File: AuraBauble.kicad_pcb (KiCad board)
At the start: 2 copper layers, 15 x 19 mm, 39 parts, among them J1 Bauble-Expando!, J2 USB_A, J3 SWD, SW1 KXT 321 LHS, U1 ATSAMD11D14A-M, U2 LP5912-3.3DRV, U3 74LVC1G02SE-7, U4 NXB0104GU12X, Y1 FC-135R

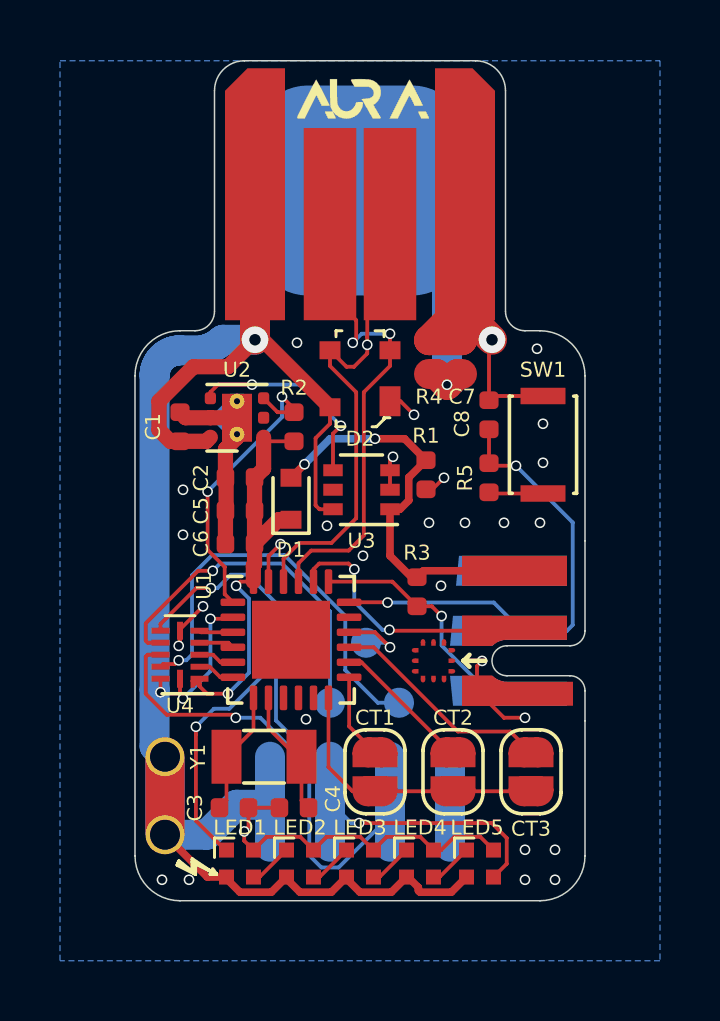
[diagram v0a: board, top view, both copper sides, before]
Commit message: Move BP1 a bit so it doesn't collide with expando silk.
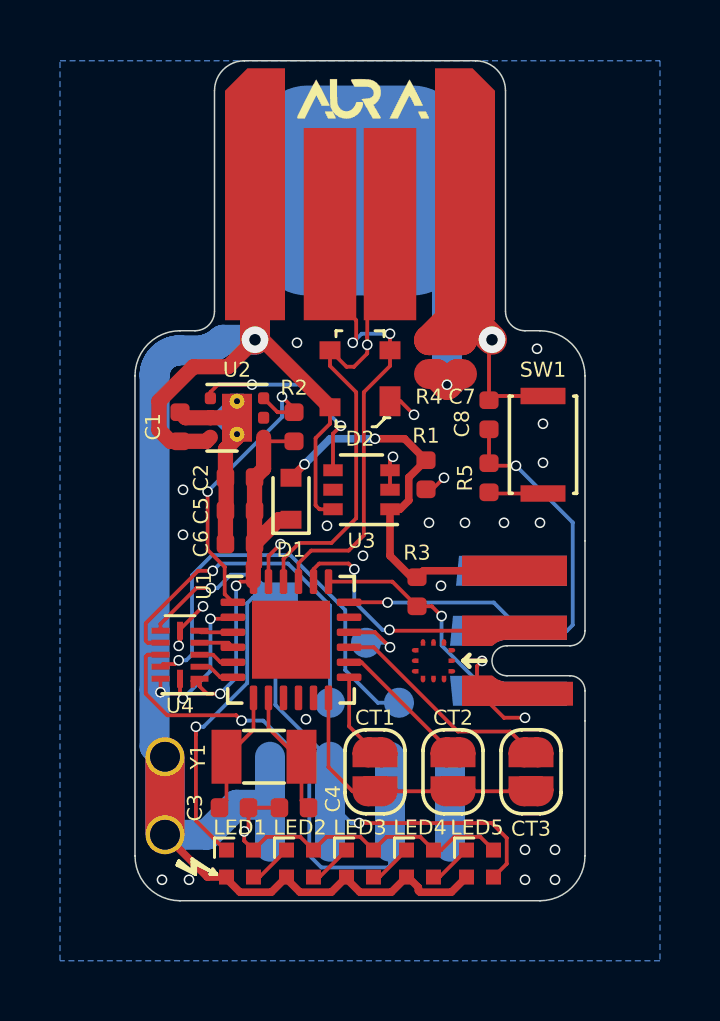
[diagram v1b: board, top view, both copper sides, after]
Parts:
- moved BP1 0.86 mm to (147.2, 68.6)
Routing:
- net /SCK_5V: track 15.2 -> 16.2 mm
- net VCC: track 14.2 -> 13.7 mm

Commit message: Cleanup some C & R values.
Adjusted C7 up slightly based on parts available. R1 moved from 100 MOhms to 1 MOhm to line up part with R4.
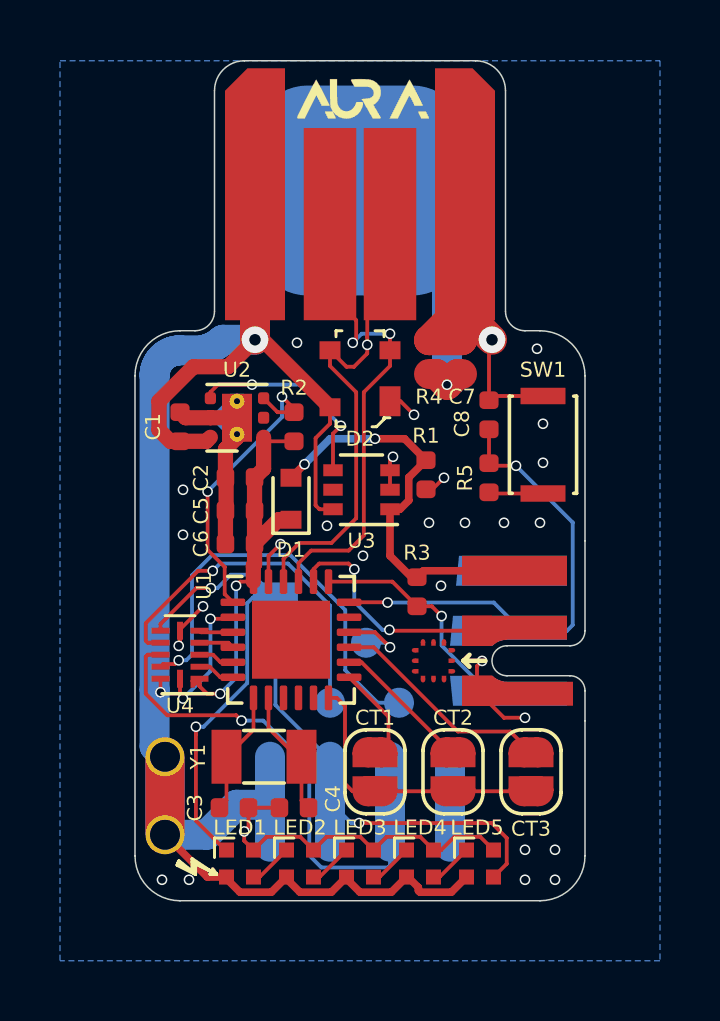
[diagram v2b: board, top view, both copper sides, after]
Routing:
- net GND: vias 30 -> 29
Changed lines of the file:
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@@
     (thickness 1.6)
     (drawings 30)
-    (tracks 440)
+    (tracks 442)
     (zones 0)
     (modules 39)
@@
   (title_block
     (title "Aura Bauble")
-    (date 2020-09-14)
+    (date 2020-09-15)
     (rev 0)
     (company cmd.wtf)
@@
     (38 B.Mask user hide)
     (39 F.Mask user hide)
-    (40 Dwgs.User user hide)
+    (40 Dwgs.User user)
     (41 Cmts.User user hide)
     (42 Eco1.User user hide)
@@
   (via (at 143.4 77.3) (size 0.3556) (drill 0.254) (layers F.Cu B.Cu) (net 3))
   (via (at 147.9 59.4) (size 0.3556) (drill 0.254) (layers F.Cu B.Cu) (net 3))
-  (via (at 148.2 71.95) (size 0.3556) (drill 0.254) (layers F.Cu B.Cu) (net 3))
   (via (at 152.7 67.5) (size 0.3556) (drill 0.254) (layers F.Cu B.Cu) (net 3))
   (via (at 150.1 66.5) (size 0.3556) (drill 0.254) (layers F.Cu B.Cu) (net 3))
@@
   (segment (start 153.1 74.35) (end 155.7 74.35) (width 0.127) (layer F.Cu) (net 10))
   (segment (start 149.752408 74.35) (end 150.5 74.35) (width 0.127) (layer F.Cu) (net 10))
-  (segment (start 148.95 73.547592) (end 149.752408 74.35) (width 0.127) (layer F.Cu) (net 10))
-  (segment (start 148.95 71.2375) (end 148.95 73.547592) (width 0.127) (layer F.Cu) (net 10))
-  (segment (start 149.6375 72.1875) (end 150.5 73.05) (width 0.127) (layer F.Cu) (net 11))
-  (segment (start 149.6375 70.55) (end 149.6375 72.1875) (width 0.127) (layer F.Cu) (net 11))
+  (segment (start 149.5 71.51) (end 149.5 74.097592) (width 0.127) (layer F.Cu) (net 10))
+  (segment (start 149.5 74.097592) (end 149.752408 74.35) (width 0.127) (layer F.Cu) (net 10))
+  (segment (start 148.95 71.2375) (end 149.2275 71.2375) (width 0.127) (layer F.Cu) (net 10))
+  (segment (start 149.2275 71.2375) (end 149.5 71.51) (width 0.127) (layer F.Cu) (net 10))
+  (segment (start 149.6375 70.55) (end 150.95 71.8625) (width 0.127) (layer F.Cu) (net 11))
+  (segment (start 150.95 72.6) (end 150.5 73.05) (width 0.127) (layer F.Cu) (net 11))
+  (segment (start 150.95 71.8625) (end 150.95 72.6) (width 0.127) (layer F.Cu) (net 11))
   (segment (start 153.05 73.05) (end 153.1 73.05) (width 0.127) (layer F.Cu) (net 12))
   (segment (start 150.05 70.05) (end 153.05 73.05) (width 0.127) (layer F.Cu) (net 12))
